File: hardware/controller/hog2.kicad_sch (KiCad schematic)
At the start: 59 parts, among them J10 Conn_01x01, J11 Conn_01x01, J12 Conn_01x03, J13 Conn_01x03, J9 Conn_01x01, Q10 YJD60N04A, Q11 YJD60N04A, Q12 YJD60N04A, Q13 YJD60N04A, Q8 YJD60N04A, Q9 YJD60N04A, U15 LM2105D, U16 LMV331, U17 LM2105D, U18 LMV331, U19 LM2105D, U20 LMV331

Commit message: footprints, layout
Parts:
- removed J12, J13: Conn_01x03, symbol Connector_Generic:Conn_01x03
- removed Q10, Q11, Q12, Q13, Q8, Q9: YJD60N04A, symbol Simulation_SPICE:NMOS
- added J12: Conn_02x03_Odd_Even, Connector_PinHeader_2.54mm:PinHeader_2x03_P2.54mm_Horizontal, symbol Connector_Generic:Conn_02x03_Odd_Even
- added Q10, Q11, Q12, Q13, Q8, Q9: AOD66406, Package_TO_SOT_SMD:TO-252-2, symbol Device:Q_NMOS_DGS
- C57: renamed from C55; footprint (none) -> Capacitor_SMD:C_0603_1608Metric
- C58: renamed from C56; footprint (none) -> Capacitor_SMD:C_0603_1608Metric
- C59: renamed from C57; footprint (none) -> Capacitor_SMD:C_0603_1608Metric
- C60: renamed from C58; footprint (none) -> Capacitor_SMD:CP_Elec_6.3x7.7
- C61: renamed from C59; footprint (none) -> Capacitor_SMD:C_0603_1608Metric
- C62: renamed from C60; footprint (none) -> Capacitor_SMD:C_0603_1608Metric
- C63: renamed from C61; footprint (none) -> Capacitor_SMD:C_0603_1608Metric
- C64: renamed from C62; footprint (none) -> Capacitor_SMD:C_0603_1608Metric
- C65: renamed from C63; footprint (none) -> Capacitor_SMD:CP_Elec_6.3x7.7
- C66: renamed from C64; footprint (none) -> Capacitor_SMD:C_0603_1608Metric
- C67: renamed from C65; footprint (none) -> Capacitor_SMD:C_0603_1608Metric
- C68: renamed from C66; footprint (none) -> Capacitor_SMD:C_0603_1608Metric
- C69: renamed from C67; footprint (none) -> Capacitor_SMD:C_0603_1608Metric
- C70: renamed from C68; footprint (none) -> Capacitor_SMD:CP_Elec_6.3x7.7
- C71: renamed from C69; footprint (none) -> Capacitor_SMD:C_0603_1608Metric
- C72: renamed from C70; footprint (none) -> Capacitor_SMD:C_0603_1608Metric
- C73: renamed from C71; footprint (none) -> Capacitor_SMD:C_0603_1608Metric
- C74: renamed from C72; footprint (none) -> Capacitor_SMD:C_0603_1608Metric
- C75: footprint (none) -> Capacitor_SMD:C_0603_1608Metric
- C76: renamed from C74; footprint (none) -> Capacitor_SMD:C_0603_1608Metric
- C77: renamed from C73; footprint (none) -> Capacitor_SMD:C_0603_1608Metric
- J10, J11, J9: footprint (none) -> Connector_Wire:SolderWire-2.5sqmm_1x01_D2.4mm_OD4.4mm
- JP4, JP5, JP6: footprint (none) -> Jumper:SolderJumper-3_P1.3mm_Open_RoundedPad1.0x1.5mm
- R37, R38, R39, R40, R41, R42, R43, R44, R45, R46, R47, R48, R49, R50, R51, R52, R53, R54: footprint (none) -> Resistor_SMD:R_0603_1608Metric
- U15: renamed from U16; footprint (none) -> Package_TO_SOT_SMD:SOT-23-5
- U17: renamed from U18; footprint (none) -> Package_TO_SOT_SMD:SOT-23-5
- U19: renamed from U20; footprint (none) -> Package_TO_SOT_SMD:SOT-23-5
- renumbered U15 to U14, U17 to U16, U19 to U18
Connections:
- net +5V: now also J12.3 (Pin_3), J12.4 (Pin_4)
- net GND: now also J12.5 (Pin_5), J12.6 (Pin_6), Q11.3 (S), Q13.3 (S), Q9.3 (S)
- net PHASE_U: now also Q8.3 (S), Q9.1 (D)
- net PHASE_V: now also Q10.3 (S), Q11.1 (D)
- net PHASE_W: now also Q12.3 (S), Q13.1 (D)
- net SERVO2_PWM_X: now also J12.1 (Pin_1)
- net SERVO2_PWM_Y: now also J12.2 (Pin_2)
- net VBUS: now also Q10.1 (D), Q12.1 (D), Q8.1 (D)
- net at R50.2: now also Q12.2 (G)
- net at R41.2: now also Q9.2 (G)
- net at R54.2: now also Q13.2 (G)
- net at R37.2: now also Q8.2 (G)
- net at R43.2: now also Q10.2 (G)
- net at R48.2: now also Q11.2 (G)
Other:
- moved on the sheet: C75, C76, C77

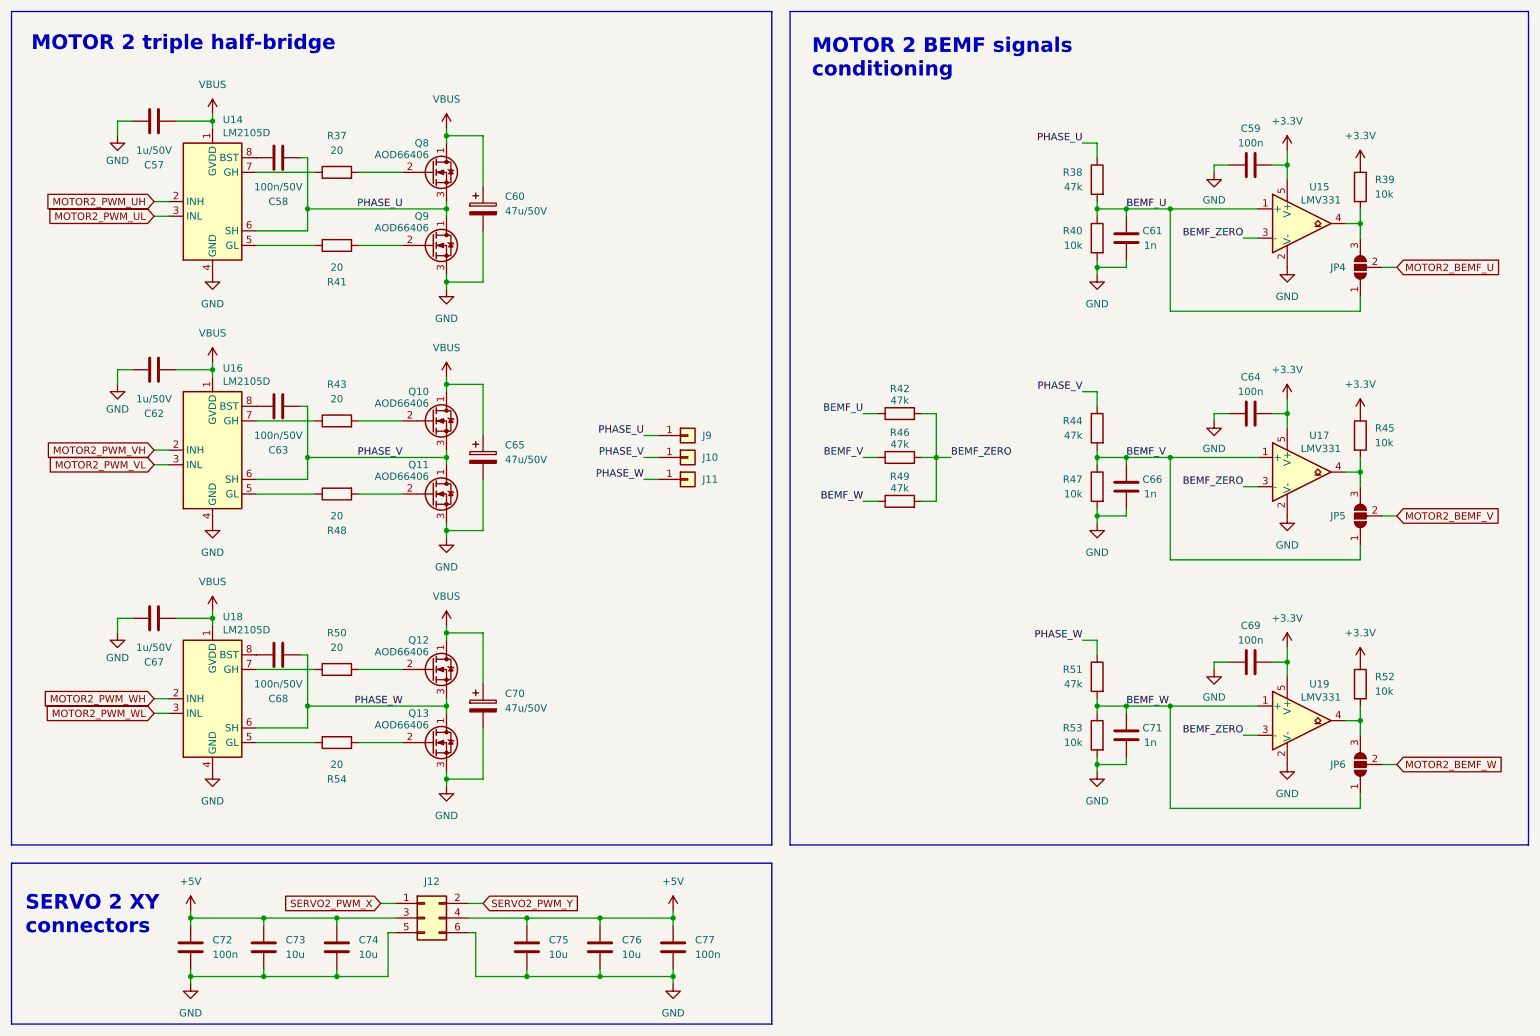
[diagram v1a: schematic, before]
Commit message: add VBUS sense to STM and ESP, change buttons and sw to vertical, add USB-C to SEM
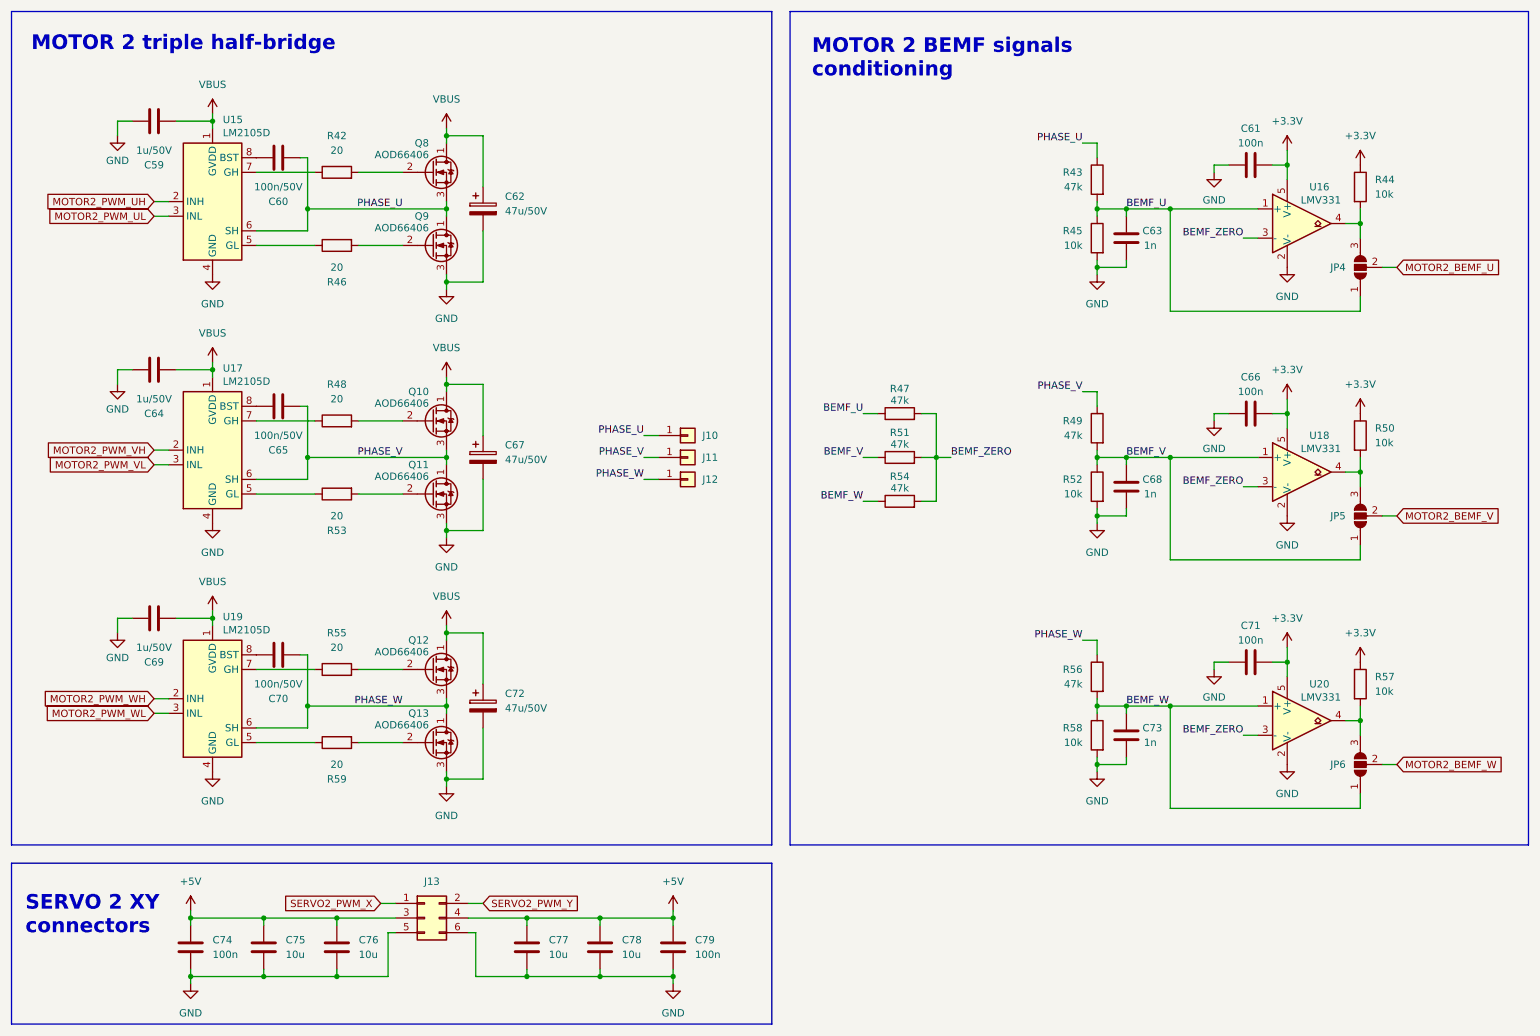
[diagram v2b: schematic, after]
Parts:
- renumbered C57 to C59, C58 to C60, C59 to C61, C60 to C62, C61 to C63, C62 to C64, C63 to C65, C64 to C66, C65 to C67, C66 to C68, C67 to C69, C68 to C70, C69 to C71, C70 to C72, C71 to C73, C72 to C74, C73 to C75, C74 to C76, C75 to C77, C76 to C78, C77 to C79, J9 to J10, J10 to J11, J11 to J12, J12 to J13, R37 to R42, R38 to R43, R39 to R44, R40 to R45, R41 to R46, R42 to R47, R43 to R48, R44 to R49, R45 to R50, R46 to R51, R47 to R52, R48 to R53, R49 to R54, R50 to R55, R51 to R56, R52 to R57, R53 to R58, R54 to R59, U14 to U15, U15 to U16, U16 to U17, U17 to U18, U18 to U19, U19 to U20

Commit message: USBLC6, IR2101
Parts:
- removed U15, U17, U19: LM2105D, Package_SO:SOIC-8_3.9x4.9mm_P1.27mm, symbol Driver_FET:LM2105D
- added D10, D11, D9: 1N5819HW-7-F, Diode_SMD:Nexperia_CFP3_SOD-123W, symbol Device:D_Schottky
- added U15, U17, U19: IR2101, Package_SO:SOIC-8_3.9x4.9mm_P1.27mm, symbol Driver_FET:IR2101
- C60, C65, C70: value 100n/50V -> 1u/50V
- R42, R46, R48, R53, R55, R59: value 20 -> 100
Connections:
- net GND: now also U15.4 (COM), U17.4 (COM), U19.4 (COM)
- net MOTOR2_PWM_UH: now also U15.2 (HIN)
- net MOTOR2_PWM_UL: now also U15.3 (LIN)
- net MOTOR2_PWM_VH: now also U17.2 (HIN)
- net MOTOR2_PWM_VL: now also U17.3 (LIN)
- net MOTOR2_PWM_WH: now also U19.2 (HIN)
- net MOTOR2_PWM_WL: now also U19.3 (LIN)
- net PHASE_U: now also U15.6 (VS)
- net PHASE_V: now also U17.6 (VS)
- net PHASE_W: now also U19.6 (VS)
- net VBUS: now also D10.2 (A), D11.2 (A), D9.2 (A), U15.1 (VCC), U17.1 (VCC), U19.1 (VCC)
- net at C65.1: now also D10.1 (K), U17.8 (VB)
- net at R46.1: now also U15.5 (LO)
- net at R59.1: now also U19.5 (LO)
- net at R55.1: now also U19.7 (HO)
- net at C70.1: now also D11.1 (K), U19.8 (VB)
- net at C60.1: now also D9.1 (K), U15.8 (VB)
- net at R42.1: now also U15.7 (HO)
- net at R53.1: now also U17.5 (LO)
- net at R48.1: now also U17.7 (HO)
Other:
- moved on the sheet: C62, C67, C72, Q10, Q11, Q12, Q13, Q8, Q9, R42

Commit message: custom footprints with all 3D models
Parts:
- renumbered C59 to C57, C60 to C58, C61 to C59, C62 to C60, C63 to C61, C64 to C62, C65 to C63, C66 to C64, C67 to C65, C68 to C66, C69 to C67, C70 to C68, C71 to C69, C72 to C70, C73 to C71, C74 to C72, C75 to C73, C76 to C74, C77 to C75, C78 to C76, C79 to C77

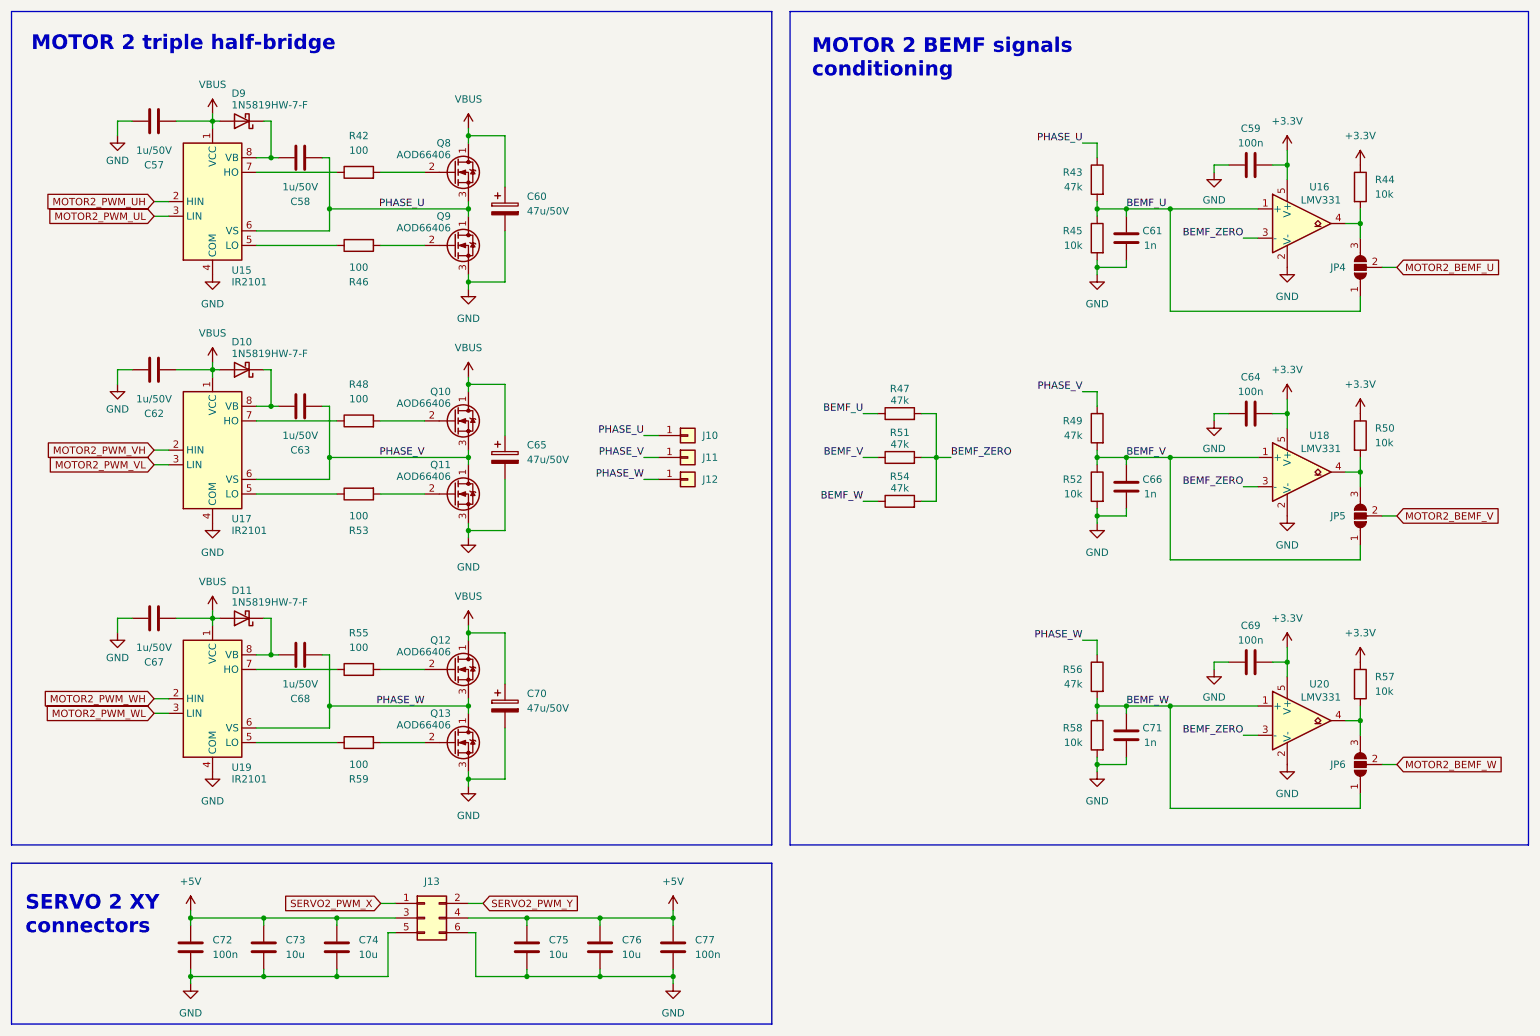
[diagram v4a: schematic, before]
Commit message: back to LM2105, remove USB-C from STM
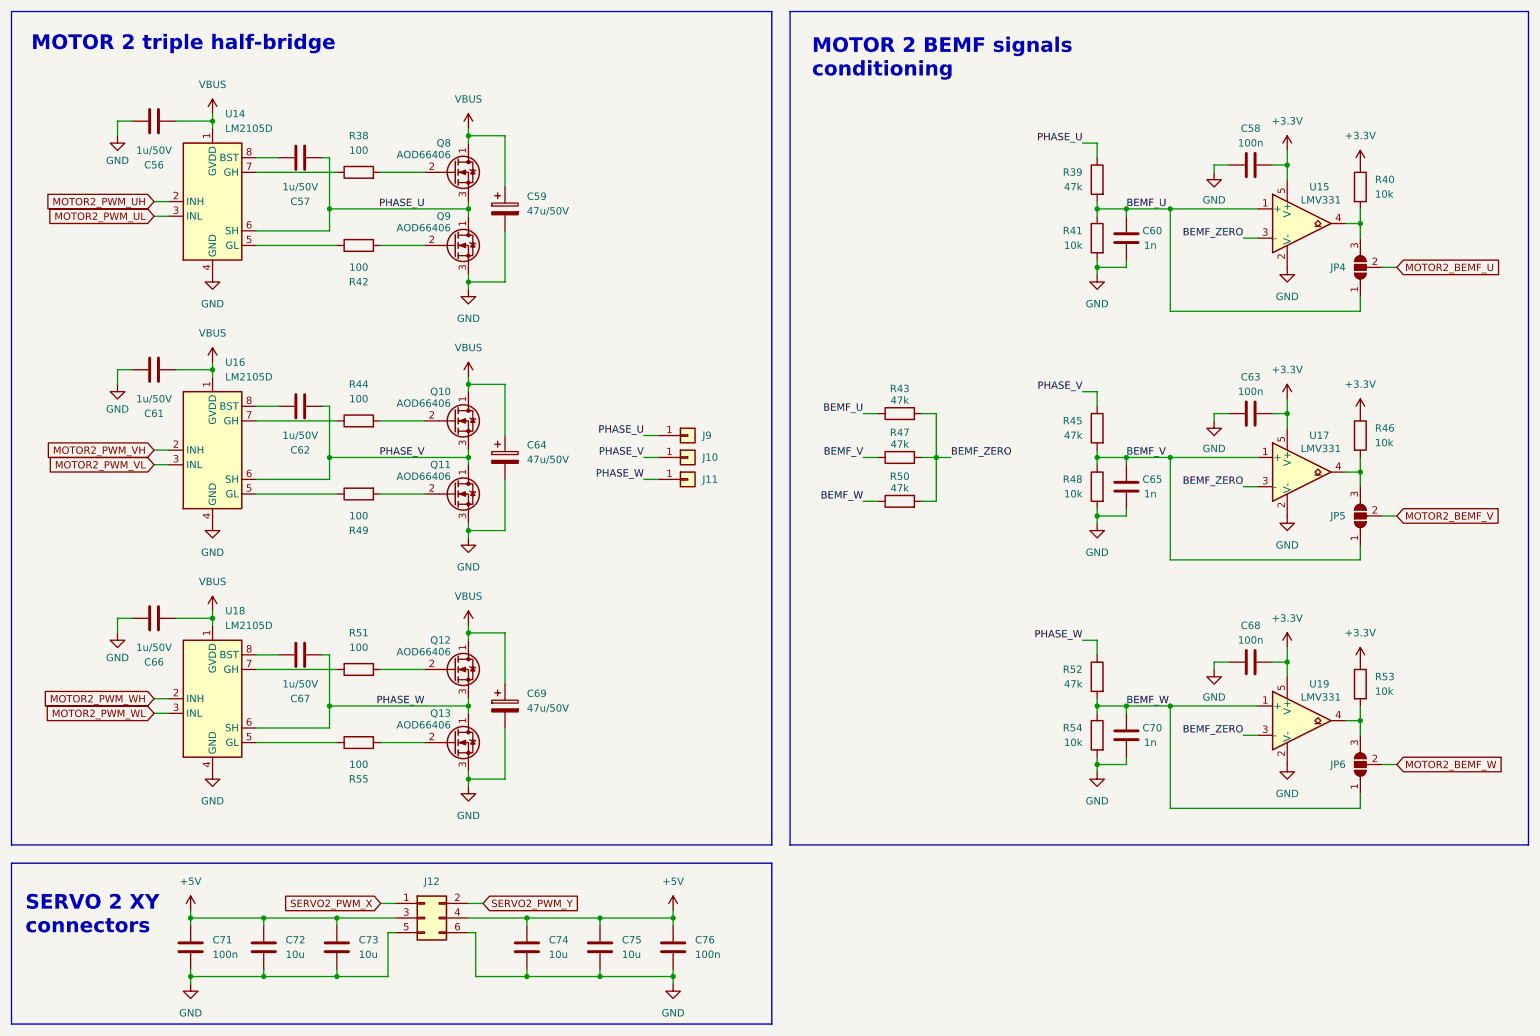
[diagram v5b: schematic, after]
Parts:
- removed D10, D11, D9: 1N5819HW-7-F, Diode_SMD:Nexperia_CFP3_SOD-123W, symbol Device:D_Schottky
- removed U15, U17, U19: IR2101, Package_SO:SOIC-8_3.9x4.9mm_P1.27mm, symbol Driver_FET:IR2101
- added U14, U16, U18: LM2105D, Package_SO:SOIC-8_3.9x4.9mm_P1.27mm, symbol Driver_FET:LM2105D
- renumbered C57 to C56, C58 to C57, C59 to C58, C60 to C59, C61 to C60, C62 to C61, C63 to C62, C64 to C63, C65 to C64, C66 to C65, C67 to C66, C68 to C67, C69 to C68, C70 to C69, C71 to C70, C72 to C71, C73 to C72, C74 to C73, C75 to C74, C76 to C75, C77 to C76, J11 to J10, J12 to J11, J13 to J12, J10 to J9, R42 to R38, R43 to R39, R44 to R40, R45 to R41, R46 to R42, R47 to R43, R48 to R44, R49 to R45, R50 to R46, R51 to R47, R52 to R48, R53 to R49, R54 to R50, R55 to R51, R56 to R52, R57 to R53, R58 to R54, R59 to R55, U16 to U15, U18 to U17, U20 to U19
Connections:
- net GND: now also U14.4 (GND), U16.4 (GND), U18.4 (GND)
- net MOTOR2_PWM_UH: now also U14.2 (INH)
- net MOTOR2_PWM_UL: now also U14.3 (INL)
- net MOTOR2_PWM_VH: now also U16.2 (INH)
- net MOTOR2_PWM_VL: now also U16.3 (INL)
- net MOTOR2_PWM_WH: now also U18.2 (INH)
- net MOTOR2_PWM_WL: now also U18.3 (INL)
- net PHASE_U: now also U14.6 (SH)
- net PHASE_V: now also U16.6 (SH)
- net PHASE_W: now also U18.6 (SH)
- net VBUS: now also U14.1 (GVDD), U16.1 (GVDD), U18.1 (GVDD)
- net at C62.1: now also U16.8 (BST)
- net at R49.1: now also U16.5 (GL)
- net at R55.1: now also U18.5 (GL)
- net at R51.1: now also U18.7 (GH)
- net at C67.1: now also U18.8 (BST)
- net at R38.1: now also U14.7 (GH)
- net at R44.1: now also U16.7 (GH)
- net at C57.1: now also U14.8 (BST)
- net at R42.1: now also U14.5 (GL)
